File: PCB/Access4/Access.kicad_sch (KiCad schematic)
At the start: 76 parts, among them J1 USB-C, J2 RFID, J3 INPUTS, J4 Shelly, J5 POWER, J6 DOOR2, J7 DOOR1, Q1 NX7002AK, Q2 PMF250XNEX, SW1 ESE13V01D, U1 ESP32-PICO-MINI-02, U2 FT231XQ, U3 G3VM-41GR8, U4 LMR16006XDDCR, U5 LMR16006XDDCR, U6 AA, U7 QR, U8 G3VM-41GR8, U9 AA

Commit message: Started on Access4
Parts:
- removed C1: 0.1uF, RevK:C_0603, symbol Device:C
- removed C10, C13: 2.2uF, RevK:C_0805_, symbol RevK:Hidden
- removed C11, C14: 10uF, RevK:C_0805_, symbol RevK:Hidden
- removed C12, C9: 100nF, RevK:C_0603_, symbol RevK:Hidden
- removed C15: 1uF, RevK:C_0603, symbol Device:C
- removed C16: 10nF, RevK:C_0603, symbol Device:C
- removed D6, D7: Schottky, RevK:D_1206_, symbol RevK:Hidden
- removed J4: Shelly, RevK:Shelly, symbol RevK:Shelly
- removed L1, L2: 6.8uH, RevK:L_4x4_, symbol RevK:Hidden
- removed Q1: NX7002AK, Package_TO_SOT_SMD:SOT-23, symbol Device:Q_NMOS_GSD
- removed R1, R3: 10k, RevK:R_0603, symbol Device:R
- removed R14, R15: 27R, RevK:R_0603, symbol Device:R
- removed R2: 4k7, RevK:R_0603, symbol Device:R
- removed R20: 100K, RevK:R_0603, symbol Device:R
- removed R21, R22: 100k 1%, RevK:R_0603, symbol Device:R
- removed R23: 18k 1%, RevK:R_0603, symbol Device:R
- removed R24: 30k 1%, RevK:R_0603, symbol Device:R
- removed U1: ESP32-PICO-MINI-02, RevK:ESP32-PICO-MINI-02, symbol RevK:ESP32-PICO-MINI-02
- removed U2: FT231XQ, RevK:QFN-20-1EP_4x4mm_P0.5mm_EP2.5x2.5mm, symbol RevK:FT231XQ
- removed U4, U5: LMR16006XDDCR, RevK:SOT-23-Thin-6-Reg, symbol RevK:LMR16006XDDCR
- added C1, C21: 10uF 50V, RevK:C_0603_, symbol RevK:Hidden
- added C15, C22: 10uF 6.3V, RevK:C_0603_, symbol RevK:Hidden
- added C16, C23: 100nF, RevK:C_0603_, symbol RevK:Hidden
- added C18: 100nF, RevK:C_0402, symbol Device:C
- added C19: 22uF, RevK:C_0402, symbol Device:C
- added C20: 1uF, RevK:C_0402, symbol Device:C
- added J8: Shelly, RevK:Shelly, symbol RevK:Shelly
- added L3, L4: 10uH, RevK:L_4x4_, symbol RevK:Hidden
- added PCB1: 70x70, RevK:PCB7070, symbol RevK:PCB
- added R1, R14: 124k, RevK:R_0402_, symbol RevK:Hidden
- added R15: 39k2, RevK:R_0402_, symbol RevK:Hidden
- added R2: 23k2, RevK:R_0402_, symbol RevK:Hidden
- added R26: 10K, RevK:R_0402, symbol Device:R
- added R27: 1M, RevK:R_0402_, symbol RevK:Hidden
- added U1, U2: MD8942, RevK:SOT-23-6-MD8942, symbol RevK:MD89420-RegBlock
- added U10: ESP32-S3-MINI-1, RevK:ESP32-S3-MINI-1, symbol RevK:ESP32-S3-MINI-1-N4R2
- added V1, V2: ~, RevK:VCUT70, symbol RevK:VCUT
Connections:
- net +12V: now also U1.5 (VIN), U2.5 (VIN)
- net +3.3V: now also C18.1, C19.1, J8.3 (3V3), R26.1, U10.3 (3V3), U2.8 (VOUT)
- net +5V: now also U1.8 (VOUT)
- net D+: now also J1.A6 (D+), J1.B6 (D+), U10.24 (GPIO20)
- net D-: now also J1.A7 (D-), J1.B7 (D-), U10.23 (GPIO19)
- net GND: now also C18.2, C19.2, C20.2, J8.1 (GND), U1.2 (GND), U1.7 (GND), U10.1 (GND), U10.2 (GND), U10.42 (GND), U10.43 (GND), U10.46 (GND), U10.47 (GND), U10.48 (GND), U10.49 (GND), U10.50 (GND), U10.51 (GND), U10.52 (GND), U10.53 (GND), U10.54 (GND), U10.55 (GND), U10.56 (GND), U10.57 (GND), U10.58 (GND), U10.59 (GND), U10.60 (GND), U10.61 (GND), U10.62 (GND), U10.63 (GND), U10.64 (GND), U10.65 (GND), U2.2 (GND), U2.7 (GND)
- net SHDN: now also U1.4 (EN)
- new net: J8.5 (Tx), U10.39 (GPIO43)
- new net: J8.2 (0), U10.4 (GPIO0)
- new net: J8.4 (Rx), U10.40 (GPIO44)
- new net: C20.1, R26.2, U10.45 (EN)
- no-connect marks 13 -> 1
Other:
- note added: "Use FET for polarity?"

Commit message: Tweak
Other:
- note added: "Use FET for polarity? 0402s"
- note removed: "Use FET for polarity?"
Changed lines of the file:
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@@
     (effects (font (size 1.27 1.27)) (justify left bottom))
   )
-  (text "Use FET for polarity?" (at 223.52 22.86 0)
+  (text "Use FET for polarity?\n\n0402s" (at 223.52 22.86 0)
     (effects (font (size 1.27 1.27)) (justify left bottom))
   )

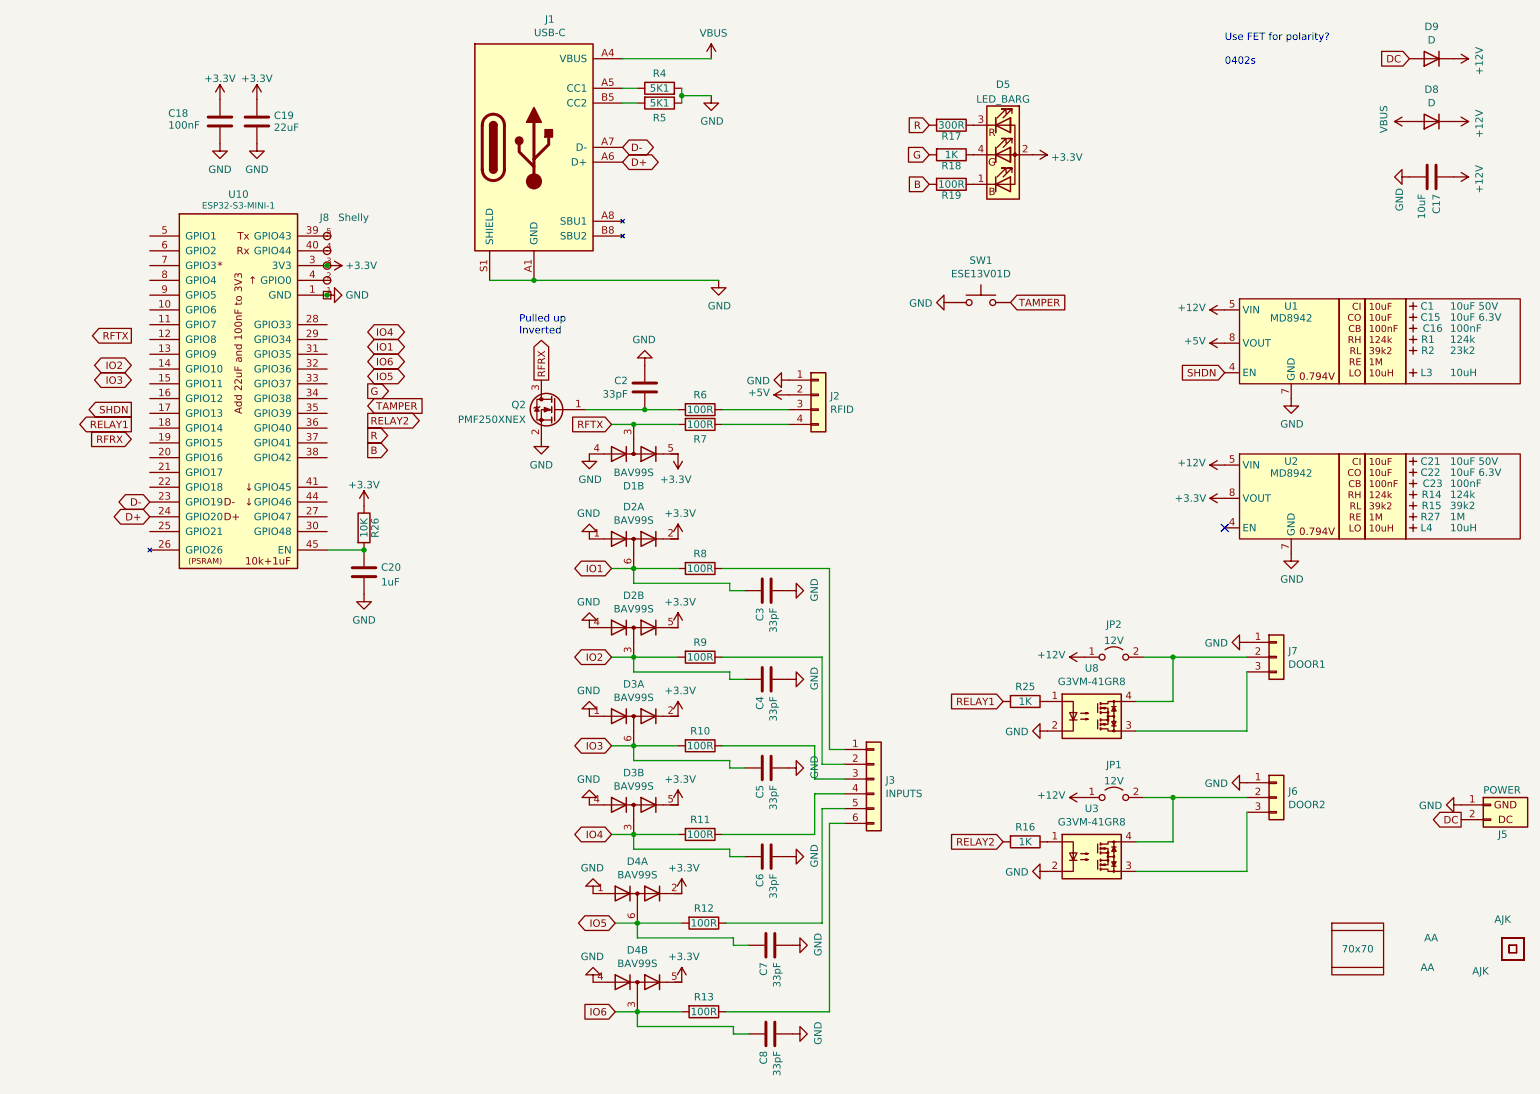
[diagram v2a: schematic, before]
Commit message: Basic size and placement
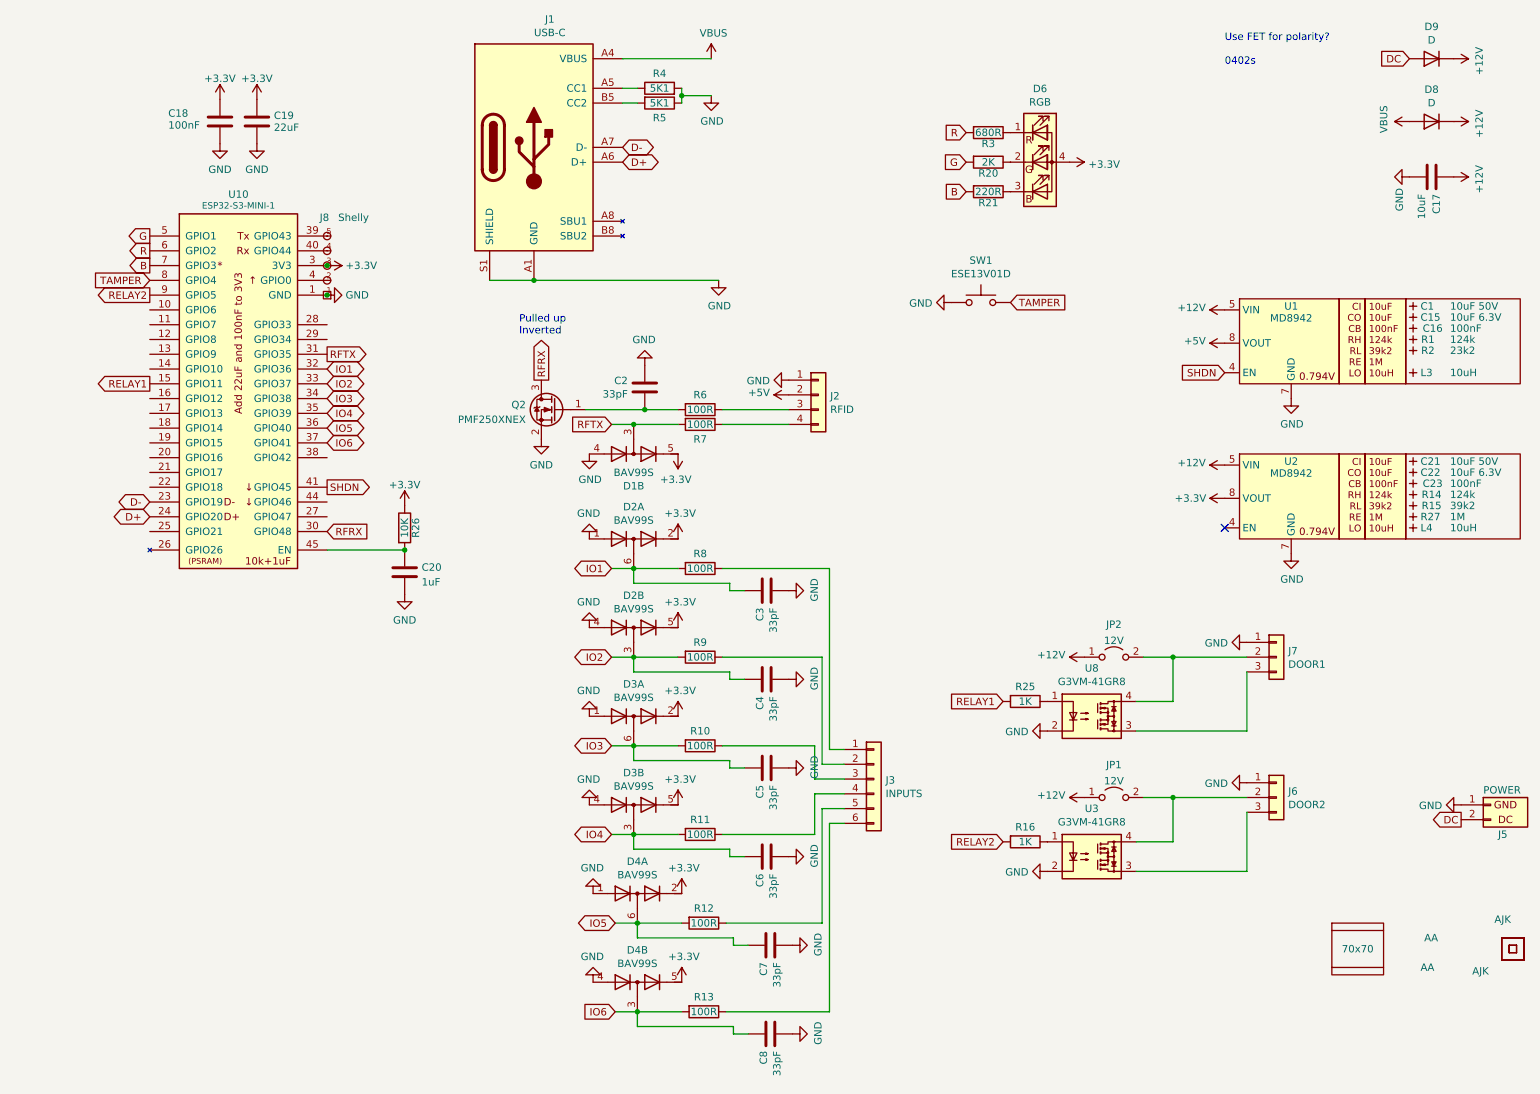
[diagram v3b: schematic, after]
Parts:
- removed D5: LED_BARG, RevK:MHS190RGBCT, symbol Device:LED_BARG
- removed R17: 300R, RevK:R_0603, symbol Device:R
- removed R18: 1K, RevK:R_0603, symbol Device:R
- removed R19: 100R, RevK:R_0603, symbol Device:R
- added D6: RGB, RevK:LED-RGB-1.6x1.6, symbol Device:LED_RGBA
- added R20: 2K, RevK:R_0402, symbol Device:R
- added R21: 220R, RevK:R_0402, symbol Device:R
- added R3: 680R, RevK:R_0402, symbol Device:R
- C17: footprint RevK:C_0805 -> RevK:C_0402
- C2, C3, C4, C5, C6, C7, C8: footprint RevK:C_0603 -> RevK:C_0402
- D1, D2, D3, D4: footprint Package_TO_SOT_SMD:SOT-363_SC-70-6 -> RevK:SOT-363_SC-70-6
- R10, R11, R12, R13, R16, R25, R4, R5, R6, R7, R8, R9: footprint RevK:R_0603 -> RevK:R_0402
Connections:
- net +3.3V: now also D6.4 (A)
- net B: now also U10.7 (GPIO3), R21.2
- net G: now also U10.5 (GPIO1), R20.2
- net IO1: now also U10.32 (GPIO36)
- net IO2: now also U10.33 (GPIO37)
- net IO3: now also U10.34 (GPIO38)
- net IO4: now also U10.35 (GPIO39)
- net IO5: now also U10.36 (GPIO40)
- net IO6: now also U10.37 (GPIO41)
- net R: now also U10.6 (GPIO2), R3.2
- net RELAY1: now also U10.15 (GPIO11)
- net RELAY2: now also U10.9 (GPIO5)
- net RFRX: now also U10.30 (GPIO48)
- net RFTX: now also U10.31 (GPIO35)
- net SHDN: now also U10.41 (GPIO45)
- net TAMPER: now also U10.8 (GPIO4)
- new net: D6.3 (BK), R21.1
- new net: D6.1 (RK), R3.1
- new net: D6.2 (GK), R20.1
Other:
- moved on the sheet: C20, R26

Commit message: Basic layout better
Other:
- moved on the sheet: J3
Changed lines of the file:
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@@
     (stroke (width 0) (type default))
   )
-  (wire (pts (xy 137.16 154.94) (xy 153.035 154.94))
+  (wire (pts (xy 137.16 154.94) (xy 154.94 154.94))
     (stroke (width 0) (type default))
   )
@@
     (stroke (width 0) (type default))
   )
-  (wire (pts (xy 154.305 170.18) (xy 154.305 150.495))
+  (wire (pts (xy 156.21 170.18) (xy 156.21 150.495))
     (stroke (width 0) (type default))
   )
@@
     (stroke (width 0) (type default))
   )
-  (wire (pts (xy 137.16 139.7) (xy 153.035 139.7))
+  (wire (pts (xy 137.16 139.7) (xy 154.94 139.7))
     (stroke (width 0) (type default))
   )
@@
     (stroke (width 0) (type default))
   )
-  (wire (pts (xy 155.575 140.335) (xy 158.115 140.335))
+  (wire (pts (xy 157.48 140.335) (xy 160.02 140.335))
     (stroke (width 0) (type default))
   )
@@
     (stroke (width 0) (type default))
   )
-  (wire (pts (xy 155.575 153.035) (xy 158.115 153.035))
+  (wire (pts (xy 157.48 153.035) (xy 160.02 153.035))
     (stroke (width 0) (type default))
   )
@@
     (stroke (width 0) (type default))
   )
-  (wire (pts (xy 154.305 124.46) (xy 154.305 142.875))
-    (stroke (width 0) (type default))
-  )
-  (wire (pts (xy 137.16 124.46) (xy 154.305 124.46))
+  (wire (pts (xy 156.21 124.46) (xy 156.21 142.875))
+    (stroke (width 0) (type default))
+  )
+  (wire (pts (xy 137.16 124.46) (xy 156.21 124.46))
     (stroke (width 0) (type default))
   )
@@
     (stroke (width 0) (type default))
   )
-  (wire (pts (xy 137.16 109.22) (xy 155.575 109.22))
-    (stroke (width 0) (type default))
-  )
-  (wire (pts (xy 153.035 154.94) (xy 153.035 147.955))
+  (wire (pts (xy 137.16 109.22) (xy 157.48 109.22))
+    (stroke (width 0) (type default))
+  )
+  (wire (pts (xy 154.94 154.94) (xy 154.94 147.955))
     (stroke (width 0) (type default))
   )
@@
     (stroke (width 0) (type default))
   )
-  (wire (pts (xy 154.305 150.495) (xy 158.115 150.495))
+  (wire (pts (xy 156.21 150.495) (xy 160.02 150.495))
     (stroke (width 0) (type default))
   )
@@
     (stroke (width 0) (type default))
   )
-  (wire (pts (xy 153.035 147.955) (xy 158.115 147.955))
+  (wire (pts (xy 154.94 147.955) (xy 160.02 147.955))
     (stroke (width 0) (type default))
   )
@@
     (stroke (width 0) (type default))
   )
-  (wire (pts (xy 153.035 145.415) (xy 158.115 145.415))
+  (wire (pts (xy 154.94 145.415) (xy 160.02 145.415))
     (stroke (width 0) (type default))
   )
@@
     (stroke (width 0) (type default))
   )
-  (wire (pts (xy 155.575 185.42) (xy 155.575 153.035))
+  (wire (pts (xy 157.48 185.42) (xy 157.48 153.035))
     (stroke (width 0) (type default))
   )
@@
     (stroke (width 0) (type default))
   )
-  (wire (pts (xy 153.035 139.7) (xy 153.035 145.415))
+  (wire (pts (xy 154.94 139.7) (xy 154.94 145.415))
     (stroke (width 0) (type default))
   )
@@
     (stroke (width 0) (type default))
   )
-  (wire (pts (xy 137.795 185.42) (xy 155.575 185.42))
-    (stroke (width 0) (type default))
-  )
-  (wire (pts (xy 137.795 170.18) (xy 154.305 170.18))
+  (wire (pts (xy 137.795 185.42) (xy 157.48 185.42))
+    (stroke (width 0) (type default))
+  )
+  (wire (pts (xy 137.795 170.18) (xy 156.21 170.18))
     (stroke (width 0) (type default))
   )
@@
     (stroke (width 0) (type default))
   )
-  (wire (pts (xy 155.575 109.22) (xy 155.575 140.335))
+  (wire (pts (xy 157.48 109.22) (xy 157.48 140.335))
     (stroke (width 0) (type default))
   )
@@
     (stroke (width 0) (type default))
   )
-  (wire (pts (xy 154.305 142.875) (xy 158.115 142.875))
+  (wire (pts (xy 156.21 142.875) (xy 160.02 142.875))
     (stroke (width 0) (type default))
   )
@@
     )
   )
-  (symbol (lib_id "Connector_Generic:Conn_01x06") (at 163.195 145.415 0) (unit 1)
-    (in_bom yes) (on_board yes) (dnp no)
-    (property "Reference" "J3" (at 165.227 145.6182 0)
-      (effects (font (size 1.27 1.27)) (justify left))
-    )
-    (property "Value" "INPUTS" (at 165.227 147.9296 0)
-      (effects (font (size 1.27 1.27)) (justify left))
-    )
-    (property "Footprint" "RevK:PTSM-HH-6-RA" (at 163.195 145.415 0)
-      (effects (font (size 1.27 1.27)) hide)
-    )
-    (property "Datasheet" "~" (at 163.195 145.415 0)
+  (symbol (lib_id "Connector_Generic:Conn_01x06") (at 165.1 145.415 0) (unit 1)
+    (in_bom yes) (on_board yes) (dnp no)
+    (property "Reference" "J3" (at 167.132 145.6182 0)
+      (effects (font (size 1.27 1.27)) (justify left))
+    )
+    (property "Value" "INPUTS" (at 167.132 147.9296 0)
+      (effects (font (size 1.27 1.27)) (justify left))
+    )
+    (property "Footprint" "RevK:PTSM-HH-6-RA" (at 165.1 145.415 0)
+      (effects (font (size 1.27 1.27)) hide)
+    )
+    (property "Datasheet" "~" (at 165.1 145.415 0)
       (effects (font (size 1.27 1.27)) hide)
     )
@@
       (effects (font (size 1.27 1.27)) hide)
     )
-    (property "Value" "GND" (at 152.9842 112.903 0)
+    (property "Value" "GND" (at 153.035 113.03 0)
       (effects (font (size 1.27 1.27)))
     )
@@
       (effects (font (size 1.27 1.27)) hide)
     )
-    (property "Value" "GND" (at 152.9842 128.143 0)
+    (property "Value" "GND" (at 153.035 128.27 0)
       (effects (font (size 1.27 1.27)))
     )
@@
       (effects (font (size 1.27 1.27)) hide)
     )
-    (property "Value" "GND" (at 152.9842 143.383 0)
+    (property "Value" "GND" (at 153.035 143.51 0)
       (effects (font (size 1.27 1.27)))
     )
@@
       (effects (font (size 1.27 1.27)) hide)
     )
-    (property "Value" "GND" (at 152.9842 158.623 0)
+    (property "Value" "GND" (at 153.035 158.75 0)
       (effects (font (size 1.27 1.27)))
     )
@@
       (effects (font (size 1.27 1.27)) hide)
     )
-    (property "Value" "GND" (at 153.6192 173.863 0)
+    (property "Value" "GND" (at 153.035 173.99 0)
       (effects (font (size 1.27 1.27)))
     )
@@
       (effects (font (size 1.27 1.27)) hide)
     )
-    (property "Value" "GND" (at 153.6192 189.103 0)
-      (effects (font (size 1.27 1.27)))
-    )
+    (property "Value" "GND" (at 153.035 189.23 0)
+      (effects (font (size 1.27 1.27)))
+    )

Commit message: Tracked (not pretty yet).
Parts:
- removed AJK1: AJK, RevK:AJK, symbol RevK:AJK
- removed U6: AA, RevK:AA, symbol RevK:AA
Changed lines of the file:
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@@
-    )
-  )
-  (symbol (lib_id "RevK:AJK") (at 271.78 169.545 0) (unit 1)
-    (in_bom no) (on_board yes) (dnp no)
-    (property "Reference" "AJK1" (at 271.78 167.005 0)
-      (effects (font (size 1.27 1.27)) hide)
-    )
-    (property "Value" "AJK" (at 269.875 169.545 0)
-      (effects (font (size 1.27 1.27)) (justify left))
-    )
-    (property "Footprint" "RevK:AJK" (at 271.78 172.085 0)
-      (effects (font (size 1.27 1.27)) hide)
-    )
-    (property "Datasheet" "" (at 271.78 172.085 0)
-      (effects (font (size 1.27 1.27)) hide)
-    )
-    (property "Note" "Non part, PCB printed" (at 271.78 169.545 0)
-      (effects (font (size 1.27 1.27)) hide)
-    )
-    (instances
-      (project "Access"
-        (path "/2a267270-6585-45e3-a633-b53049f10066"
-          (reference "AJK1") (unit 1)
-        )
-      )
     )
   )
@@
         )
       )
-    )
-  )
-  (symbol (lib_id "RevK:AA") (at 258.445 172.72 0) (unit 1)
-    (in_bom no) (on_board yes) (dnp no)
-    (property "Reference" "U6" (at 259.715 171.45 0)
-      (effects (font (size 1.27 1.27)) hide)
-    )
-    (property "Value" "AA" (at 257.81 172.72 0)
-      (effects (font (size 1.27 1.27)) (justify left))
-    )
-    (property "Footprint" "RevK:AA" (at 258.445 172.72 0)
-      (effects (font (size 1.27 1.27)) hide)
-    )
-    (property "Datasheet" "" (at 258.445 172.72 0)
-      (effects (font (size 1.27 1.27)) hide)
-    )
-    (property "Note" "Non part, PCB printed" (at 258.445 172.72 0)
-      (effects (font (size 1.27 1.27)) hide)
-    )
-    (instances
-      (project "Access"
-        (path "/2a267270-6585-45e3-a633-b53049f10066"
-          (reference "U6") (unit 1)
-        )
-      )

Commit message: Track tidy
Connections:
- net RELAY1: now also U10.12 (GPIO8); no longer U10.15 (GPIO11)
- net RELAY2: now also U10.11 (GPIO7); no longer U10.9 (GPIO5)
- net at U3.3: now also J6.2 (Pin_2), JP1.2 (B); no longer J6.3 (Pin_3)
- net at J7.2 (Pin_2), JP2.2 (B): now also U8.3; no longer U8.4
- net at J7.3 (Pin_3): now also U8.4; no longer U8.3
- new net: J6.3 (Pin_3), U3.4
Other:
- note removed: "Use FET for polarity? 0402s"
- moved on the sheet: J6, J7, JP1, JP2, R16, R25, U3, U8
